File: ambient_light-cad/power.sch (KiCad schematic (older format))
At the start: 16 parts

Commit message: [Modified] μF to uF and deleted Ω
표기에 혼동 및 어려움으로 인해 간략하게 변경
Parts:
- C? (x2): value 2.2μF -> 2.2uF
- C? (x4): value 47μF -> 47uF
- C?: value 0.1μF -> 100nF
- L?: value 8.2μH -> 8.2uH
- R?: value 84.5kΩ -> 84.5k
- R?: value 17.8kΩ -> 17.8k
- R?: value 100kΩ -> 100k
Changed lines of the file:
@@
 P 3550 2450
 F 0 "C?" H 3642 2496 50  0000 L CNN
-F 1 "2.2μF" H 3642 2405 50  0000 L CNN
+F 1 "2.2uF" H 3642 2405 50  0000 L CNN
 F 2 "" H 3550 2450 50  0001 C CNN
 F 3 "~" H 3550 2450 50  0001 C CNN
@@
 P 4050 2450
 F 0 "R?" H 4109 2496 50  0000 L CNN
-F 1 "84.5kΩ" H 4109 2405 50  0000 L CNN
+F 1 "84.5k" H 4109 2405 50  0000 L CNN
 F 2 "" H 4050 2450 50  0001 C CNN
 F 3 "~" H 4050 2450 50  0001 C CNN
@@
 P 5850 1950
 F 0 "L?" V 6035 1950 50  0000 C CNN
-F 1 "8.2μH" V 5944 1950 50  0000 C CNN
+F 1 "8.2uH" V 5944 1950 50  0000 C CNN
 F 2 "" H 5850 1950 50  0001 C CNN
 F 3 "~" H 5850 1950 50  0001 C CNN
@@
 P 6600 2450
 F 0 "C?" H 6692 2496 50  0000 L CNN
-F 1 "47μF" H 6692 2405 50  0000 L CNN
+F 1 "47uF" H 6692 2405 50  0000 L CNN
 F 2 "" H 6600 2450 50  0001 C CNN
 F 3 "~" H 6600 2450 50  0001 C CNN
@@
 P 6150 2450
 F 0 "R?" H 6209 2496 50  0000 L CNN
-F 1 "17.8kΩ" H 6209 2405 50  0000 L CNN
+F 1 "17.8k" H 6209 2405 50  0000 L CNN
 F 2 "" H 6150 2450 50  0001 C CNN
 F 3 "~" H 6150 2450 50  0001 C CNN
@@
 P 6150 2100
 F 0 "R?" H 6209 2146 50  0000 L CNN
-F 1 "100kΩ" H 6209 2055 50  0000 L CNN
+F 1 "100k" H 6209 2055 50  0000 L CNN
 F 2 "" H 6150 2100 50  0001 C CNN
 F 3 "~" H 6150 2100 50  0001 C CNN
@@
 P 7000 2450
 F 0 "C?" H 7092 2496 50  0000 L CNN
-F 1 "47μF" H 7092 2405 50  0000 L CNN
+F 1 "47uF" H 7092 2405 50  0000 L CNN
 F 2 "" H 7000 2450 50  0001 C CNN
 F 3 "~" H 7000 2450 50  0001 C CNN
@@
 P 7400 2450
 F 0 "C?" H 7492 2496 50  0000 L CNN
-F 1 "47μF" H 7492 2405 50  0000 L CNN
+F 1 "47uF" H 7492 2405 50  0000 L CNN
 F 2 "" H 7400 2450 50  0001 C CNN
 F 3 "~" H 7400 2450 50  0001 C CNN
@@
 P 7800 2450
 F 0 "C?" H 7892 2496 50  0000 L CNN
-F 1 "47μF" H 7892 2405 50  0000 L CNN
+F 1 "47uF" H 7892 2405 50  0000 L CNN
 F 2 "" H 7800 2450 50  0001 C CNN
 F 3 "~" H 7800 2450 50  0001 C CNN
@@
 P 3150 2450
 F 0 "C?" H 3242 2496 50  0000 L CNN
-F 1 "2.2μF" H 3242 2405 50  0000 L CNN
+F 1 "2.2uF" H 3242 2405 50  0000 L CNN
 F 2 "" H 3150 2450 50  0001 C CNN
 F 3 "~" H 3150 2450 50  0001 C CNN
@@
 P 2750 2450
 F 0 "C?" H 2842 2496 50  0000 L CNN
-F 1 "0.1μF" H 2842 2405 50  0000 L CNN
+F 1 "100nF" H 2842 2405 50  0000 L CNN
 F 2 "" H 2750 2450 50  0001 C CNN
 F 3 "~" H 2750 2450 50  0001 C CNN

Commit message: [Added] VIN USBVCC select logic
OP amp와 P-channel MOSFET을 이용하여 VIN과 USBVCC를 선택하여 구동되는 회로 제작
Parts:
- added Q?: Q_PMOS_GSD, symbol Device:Q_PMOS_GSD
- added R? (x2): 10k, symbol Device:R_Small_US
- added U? (x2): LM2904, symbol Amplifier_Operational:LM2904
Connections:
- net labels added: +3.3V, VBUS, VCC
- wire segments 47 -> 66
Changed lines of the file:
@@
 	3550 1750 3550 2350
 NoConn ~ 4150 1900
+$Comp
+L Device:Q_PMOS_GSD Q?
+U 1 1 5FF936A4
+P 4300 5100
+F 0 "Q?" V 4549 5100 50  0000 C CNN
+F 1 "Q_PMOS_GSD" V 4640 5100 50  0000 C CNN
+F 2 "" H 4500 5200 50  0001 C CNN
+F 3 "~" H 4300 5100 50  0001 C CNN
+	1    4300 5100
+	0    1    1    0
+$EndComp
+$Comp
+L Amplifier_Operational:LM2904 U?
+U 1 1 5FF97489
+P 3900 4350
+F 0 "U?" H 3900 4717 50  0000 C CNN
+F 1 "LM2904" H 3900 4626 50  0000 C CNN
+F 2 "" H 3900 4350 50  0001 C CNN
+F 3 "http://www.ti.com/lit/ds/symlink/lm358.pdf" H 3900 4350 50  0001 C CNN
+	1    3900 4350
+	1    0    0    -1
+$EndComp
+$Comp
+L Amplifier_Operational:LM2904 U?
+U 3 1 5FF97E09
+P 2150 4100
+F 0 "U?" H 2108 4146 50  0000 L CNN
+F 1 "LM2904" H 2108 4055 50  0000 L CNN
+F 2 "" H 2150 4100 50  0001 C CNN
+F 3 "http://www.ti.com/lit/ds/symlink/lm358.pdf" H 2150 4100 50  0001 C CNN
+	3    2150 4100
+	1    0    0    -1
+$EndComp
+$Comp
+L power:+12V #PWR?
+U 1 1 5FF9F54C
+P 2600 3600
+F 0 "#PWR?" H 2600 3450 50  0001 C CNN
+F 1 "+12V" H 2615 3773 50  0000 C CNN
+F 2 "" H 2600 3600 50  0001 C CNN
+F 3 "" H 2600 3600 50  0001 C CNN
+	1    2600 3600
+	1    0    0    -1
+$EndComp
+$Comp
+L Device:R_Small_US R?
+U 1 1 5FFA0592
+P 2600 3900
+F 0 "R?" H 2668 3946 50  0000 L CNN
+F 1 "10k" H 2668 3855 50  0000 L CNN
+F 2 "" H 2600 3900 50  0001 C CNN
+F 3 "~" H 2600 3900 50  0001 C CNN
+	1    2600 3900
+	1    0    0    -1
+$EndComp
+$Comp
+L Device:R_Small_US R?
+U 1 1 5FFA1CD1
+P 2600 4300
+F 0 "R?" H 2668 4346 50  0000 L CNN
+F 1 "10k" H 2668 4255 50  0000 L CNN
+F 2 "" H 2600 4300 50  0001 C CNN
+F 3 "~" H 2600 4300 50  0001 C CNN
+	1    2600 4300
+	1    0    0    -1
+$EndComp
+Wire Wire Line
+	2600 3800 2600 3600
+Wire Wire Line
+	2600 4600 2600 4400
+Wire Wire Line
+	4200 4350 4300 4350
+$Comp
+L power:+3.3V #PWR?
+U 1 1 5FFACE03
+P 3050 4400
+F 0 "#PWR?" H 3050 4250 50  0001 C CNN
+F 1 "+3.3V" H 3065 4573 50  0000 C CNN
+F 2 "" H 3050 4400 50  0001 C CNN
+F 3 "" H 3050 4400 50  0001 C CNN
+	1    3050 4400
+	1    0    0    -1
+$EndComp
+Wire Wire Line
+	3050 4400 3050 4450
+Wire Wire Line
+	3050 4450 3600 4450
+Wire Wire Line
+	2600 4000 2600 4100
+Wire Wire Line
+	2600 4100 3300 4100
+Wire Wire Line
+	3300 4100 3300 4250
+Wire Wire Line
+	3300 4250 3600 4250
+Connection ~ 2600 4100
+Wire Wire Line
+	2600 4100 2600 4200
+$Comp
+L power:+5V #PWR?
+U 1 1 5FFBC4EE
+P 4750 5100
+F 0 "#PWR?" H 4750 4950 50  0001 C CNN
+F 1 "+5V" H 4765 5273 50  0000 C CNN
+F 2 "" H 4750 5100 50  0001 C CNN
+F 3 "" H 4750 5100 50  0001 C CNN
+	1    4750 5100
+	1    0    0    -1
+$EndComp
+$Comp
+L power:VCC #PWR?
+U 1 1 5FFBCFCE
+P 5000 5100
+F 0 "#PWR?" H 5000 4950 50  0001 C CNN
+F 1 "VCC" H 5015 5273 50  0000 C CNN
+F 2 "" H 5000 5100 50  0001 C CNN
+F 3 "" H 5000 5100 50  0001 C CNN
+	1    5000 5100
+	1    0    0    -1
+$EndComp
+Wire Wire Line
+	4500 5200 4750 5200
+Wire Wire Line
+	5000 5200 5000 5100
+Wire Wire Line
+	4750 5100 4750 5200
+Connection ~ 4750 5200
+Wire Wire Line
+	4750 5200 5000 5200
+$Comp
+L power:VBUS #PWR?
+U 1 1 5FF95260
+P 3600 5100
+F 0 "#PWR?" H 3600 4950 50  0001 C CNN
+F 1 "VBUS" H 3615 5273 50  0000 C CNN
+F 2 "" H 3600 5100 50  0001 C CNN
+F 3 "" H 3600 5100 50  0001 C CNN
+	1    3600 5100
+	1    0    0    -1
+$EndComp
+Wire Wire Line
+	3600 5100 3600 5200
+Wire Wire Line
+	3600 5200 4100 5200
+Wire Wire Line
+	4300 4350 4300 4900
+$Comp
+L power:+5V #PWR?
+U 1 1 5FFCFE09
+P 2050 3600
+F 0 "#PWR?" H 2050 3450 50  0001 C CNN
+F 1 "+5V" H 2065 3773 50  0000 C CNN
+F 2 "" H 2050 3600 50  0001 C CNN
+F 3 "" H 2050 3600 50  0001 C CNN
+	1    2050 3600
+	1    0    0    -1
+$EndComp
+$Comp
+L power:GND #PWR?
+U 1 1 5FFD1784
+P 2600 4600
+F 0 "#PWR?" H 2600 4350 50  0001 C CNN
+F 1 "GND" H 2605 4427 50  0000 C CNN
+F 2 "" H 2600 4600 50  0001 C CNN
+F 3 "" H 2600 4600 50  0001 C CNN
+	1    2600 4600
+	1    0    0    -1
+$EndComp
+$Comp
+L power:GND #PWR?
+U 1 1 5FFD2EB4
+P 2050 4600
+F 0 "#PWR?" H 2050 4350 50  0001 C CNN
+F 1 "GND" H 2055 4427 50  0000 C CNN
+F 2 "" H 2050 4600 50  0001 C CNN
+F 3 "" H 2050 4600 50  0001 C CNN
+	1    2050 4600
+	1    0    0    -1
+$EndComp
+Wire Wire Line
+	2050 3600 2050 3800
+Wire Wire Line
+	2050 4400 2050 4600
 $EndSCHEMATC

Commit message: [Modified] Register symbol
R_Small to R_Small_US (구불구불하게 생긴 기호)
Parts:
- R? (x3): symbol Device:R_Small -> Device:R_Small_US
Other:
- moved on the sheet: R?
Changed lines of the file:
@@
 	3550 2650 3550 2550
 $Comp
-L Device:R_Small R?
+L Device:R_Small_US R?
 U 1 1 5FDC2ECB
 P 4050 2450
@@
 Connection ~ 6600 1950
 $Comp
-L Device:R_Small R?
+L Device:R_Small_US R?
 U 1 1 5FDC2EF2
 P 6150 2450
@@
 	6150 2650 6150 2550
 $Comp
-L Device:R_Small R?
+L Device:R_Small_US R?
 U 1 1 5FDC2EFF
 P 6150 2100
@@
 L Device:R_Small_US R?
 U 1 1 5FFA0592
-P 2600 3900
-F 0 "R?" H 2668 3946 50  0000 L CNN
-F 1 "10k" H 2668 3855 50  0000 L CNN
-F 2 "" H 2600 3900 50  0001 C CNN
-F 3 "~" H 2600 3900 50  0001 C CNN
-	1    2600 3900
+P 2600 3850
+F 0 "R?" H 2668 3896 50  0000 L CNN
+F 1 "10k" H 2668 3805 50  0000 L CNN
+F 2 "" H 2600 3850 50  0001 C CNN
+F 3 "~" H 2600 3850 50  0001 C CNN
+	1    2600 3850
 	1    0    0    -1
 $EndComp
@@
 L Device:R_Small_US R?
 U 1 1 5FFA1CD1
-P 2600 4300
-F 0 "R?" H 2668 4346 50  0000 L CNN
-F 1 "10k" H 2668 4255 50  0000 L CNN
-F 2 "" H 2600 4300 50  0001 C CNN
-F 3 "~" H 2600 4300 50  0001 C CNN
-	1    2600 4300
-	1    0    0    -1
-$EndComp
-Wire Wire Line
-	2600 3800 2600 3600
-Wire Wire Line
-	2600 4600 2600 4400
+P 2600 4350
+F 0 "R?" H 2668 4396 50  0000 L CNN
+F 1 "10k" H 2668 4305 50  0000 L CNN
+F 2 "" H 2600 4350 50  0001 C CNN
+F 3 "~" H 2600 4350 50  0001 C CNN
+	1    2600 4350
+	1    0    0    -1
+$EndComp
 Wire Wire Line
 	4200 4350 4300 4350
@@
 	3050 4450 3600 4450
 Wire Wire Line
-	2600 4000 2600 4100
-Wire Wire Line
 	2600 4100 3300 4100
 Wire Wire Line
@@
 Wire Wire Line
 	3300 4250 3600 4250
-Connection ~ 2600 4100
-Wire Wire Line
-	2600 4100 2600 4200
 $Comp
 L power:+5V #PWR?
@@
 Wire Wire Line
 	2050 4400 2050 4600
+Wire Wire Line
+	2600 3950 2600 4100
+Connection ~ 2600 4100
+Wire Wire Line
+	2600 4100 2600 4250
+Wire Wire Line
+	2600 3750 2600 3600
+Wire Wire Line
+	2600 4450 2600 4600
 $EndSCHEMATC

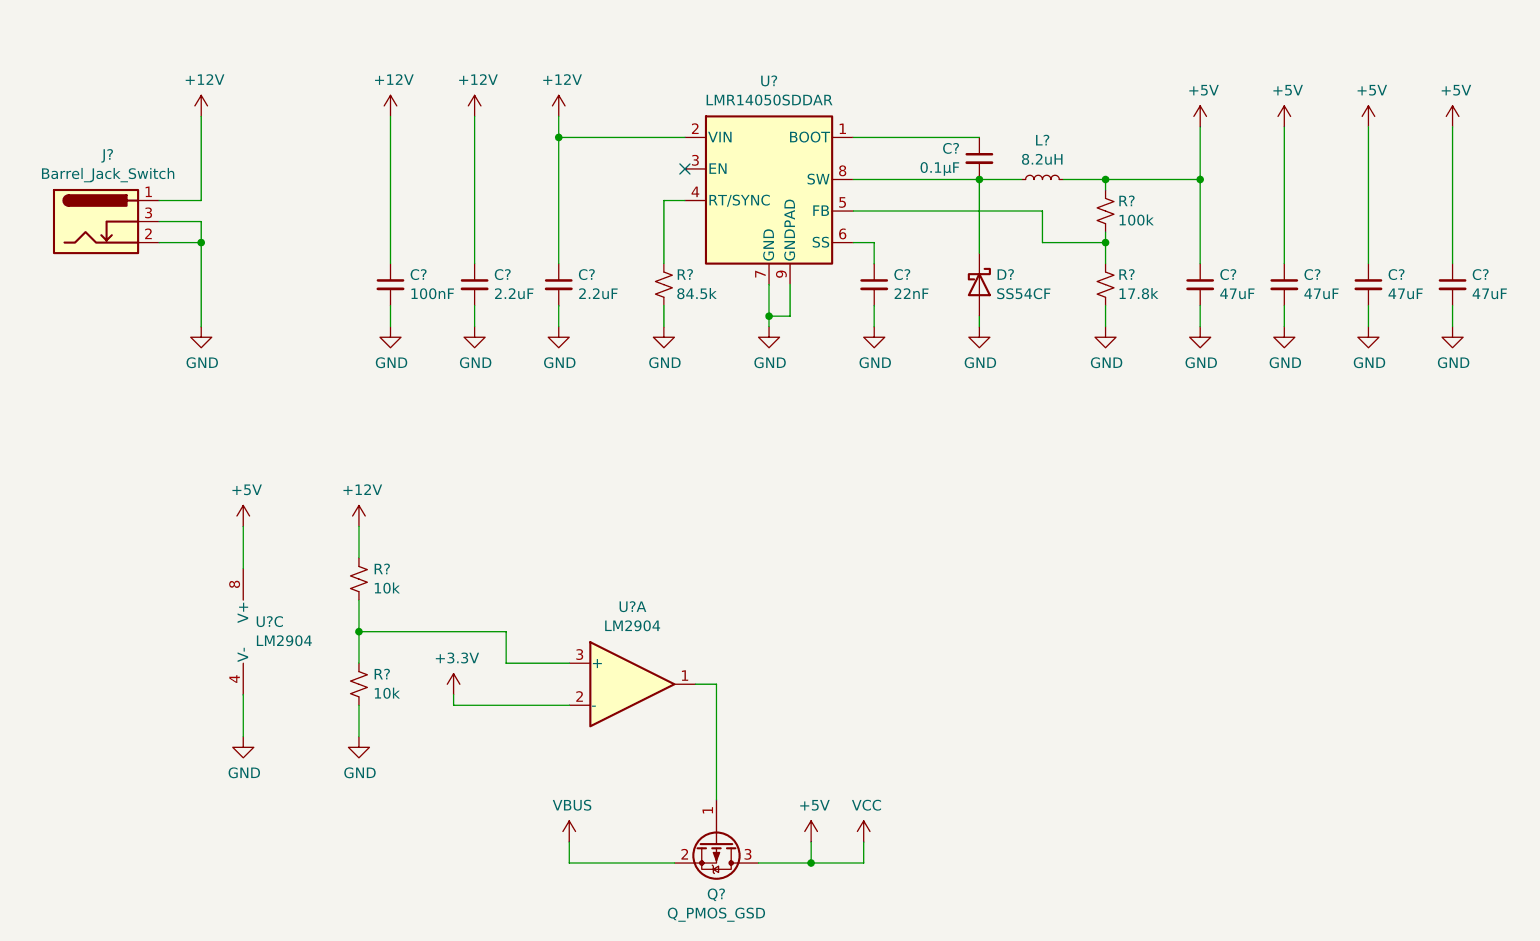
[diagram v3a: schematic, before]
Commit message: [Modified] Align and add Test Point
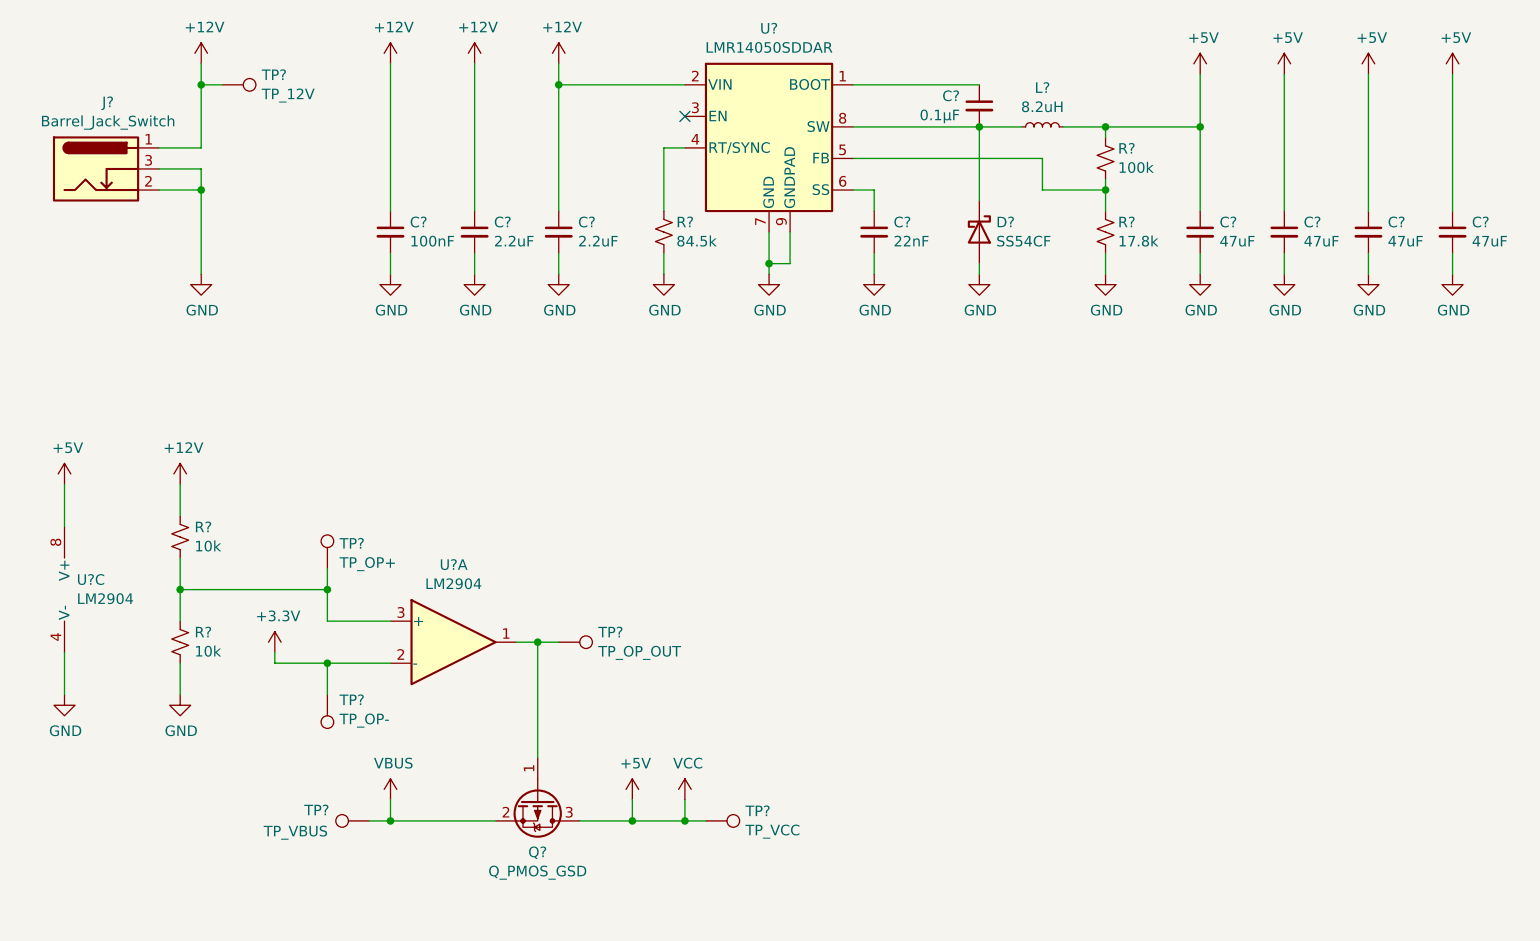
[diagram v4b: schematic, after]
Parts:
- added TP?: TP_OP+, symbol Connector:TestPoint
- added TP?: TP_OP-, symbol Connector:TestPoint
- added TP?: TP_OP_OUT, symbol Connector:TestPoint
- added TP?: TP_VBUS, symbol Connector:TestPoint
- added TP?: TP_12V, symbol Connector:TestPoint
- added TP?: TP_VCC, symbol Connector:TestPoint
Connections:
- net +12V: now also TP?.1
- net +3V3: now also TP?.1
- net +5V: now also TP?.1
- net VBUS: now also TP?.1
- net at Q?.1 (G), U?.1: now also TP?.1
- net at R?.1, R?.2, U?.3 (+): now also TP?.1
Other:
- moved on the sheet: C?, D?, J?, L?, Q?, R?, U?, U?A, U?C
